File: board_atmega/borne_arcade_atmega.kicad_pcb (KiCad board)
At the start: 2 copper layers, 0 parts

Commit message: Layout and some modifications to ease layout
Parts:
- added C1: 100nF, SM0603, F.Cu at (301.1, 151.9)
- added C2: 1uF, SM0603, F.Cu at (295.6, 143.2)
- added C3: 100nF, SM0603, F.Cu at (298.3, 135.1)
- added C4: 100nF, SM0603, F.Cu at (300.4, 134.6)
- added C5: 1uF, SM0603, F.Cu at (307.4, 135.5)
- added C6: 22pF, SM0603, F.Cu at (306.5, 156.3)
- added C7: 10uF, SM0603, F.Cu at (311.4, 146.4)
- added C8: 22pF, SM0603, F.Cu at (298.4, 156.3)
- added FB1: FILTER, SM0603, F.Cu at (291.7, 139.2)
- added G1: LOGO, LOGO_135, F.Cu at (320.9, 153.0)
- added G2: LOGO_FOL, LOGO_FOL, F.Cu at (321.1, 134.8)
- added H1: HOLE_3MM, Hole_3mm, F.Cu at (283.6, 166.3)
- added H2: HOLE_3MM, Hole_3mm, F.Cu at (283.6, 123.2)
- added H3: HOLE_3MM, Hole_3mm, F.Cu at (325.6, 144.4)
- added P1: MUSB, USB_Mini, F.Cu at (282.3, 145.0)
- added P2: CONN_15, pin_array_15x1, F.Cu at (304.4, 163.2)
- added P3: CONN_15, pin_array_15x1, F.Cu at (312.1, 125.8)
- added R1: 22, SM0603, F.Cu at (291.4, 143.4)
- added R10: 100K, SM0603, F.Cu at (308.1, 166.3)
- added R11: 100K, SM0603, F.Cu at (310.8, 166.3)
- added R12: 100K, SM0603, F.Cu at (313.2, 166.3)
- added R13: 100K, SM0603, F.Cu at (315.8, 166.3)
- added R14: 100K, SM0603, F.Cu at (318.4, 166.3)
- added R15: 100K, SM0603, F.Cu at (320.9, 166.3)
- added R16: 100K, SM0603, F.Cu at (323.4, 166.3)
- added R17: 100K, SM0603, F.Cu at (323.6, 122.7)
- added R18: 100K, SM0603, F.Cu at (321.1, 122.7)
- added R19: 100K, SM0603, F.Cu at (318.5, 122.7)
- added R2: 22, SM0603, F.Cu at (292.1, 144.9)
- added R20: 100K, SM0603, F.Cu at (315.9, 122.7)
- added R21: 100K, SM0603, F.Cu at (313.4, 122.7)
- added R22: 100K, SM0603, F.Cu at (310.9, 122.7)
- added R23: 100K, SM0603, F.Cu at (308.4, 122.7)
- added R24: 100K, SM0603, F.Cu at (305.9, 122.7)
- added R25: 100K, SM0603, F.Cu at (303.4, 122.7)
- added R26: 100K, SM0603, F.Cu at (300.8, 122.7)
- added R27: 100K, SM0603, F.Cu at (298.1, 122.7)
- added R28: 100K, SM0603, F.Cu at (295.8, 122.7)
- added R29: 100K, SM0603, F.Cu at (293.1, 122.7)
- added R3: 10K, SM0603, F.Cu at (299.1, 151.6)
- added R4: 100K, SM0603, F.Cu at (292.9, 166.3)
- added R5: 100K, SM0603, F.Cu at (295.4, 166.3)
- added R6: 100K, SM0603, F.Cu at (297.9, 166.3)
- added R7: 100K, SM0603, F.Cu at (300.5, 166.3)
- added R8: 100K, SM0603, F.Cu at (303.1, 166.3)
- added R9: 100K, SM0603, F.Cu at (305.6, 166.2)
- added U1: ATMEGA32U4, TQFP44, F.Cu at (303.2, 142.8)
- added X1: QUARTZ_CMS_4, 7B_CMS4_Quartz, F.Cu at (302.4, 155.8)
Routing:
- net DGND: track 0.00 -> 305.0 mm, vias 0 -> 46
- net N-0000033: track 0.00 -> 31.5 mm
- net N-0000034: track 0.00 -> 29.0 mm
- net N-0000015: track 0.00 -> 28.3 mm
- net N-0000035: track 0.00 -> 26.7 mm
- net N-0000014: track 0.00 -> 25.7 mm
- net N-0000031: track 0.00 -> 24.3 mm
- net N-0000013: track 0.00 -> 23.2 mm
- net N-0000030: track 0.00 -> 23.2 mm
- net N-0000028: track 0.00 -> 22.9 mm
- net N-0000027: track 0.00 -> 22.6 mm
- net N-0000029: track 0.00 -> 22.6 mm
- net N-0000012: track 0.00 -> 21.1 mm
- net N-0000032: track 0.00 -> 20.8 mm
- net N-0000023: track 0.00 -> 20.1 mm
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- added copper zone on F.Cu, net /+5V
- added copper zone on B.Cu, net DGND
- added copper zone on F.Cu, net DGND
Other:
- board outline added: 50 x 50 mm
- net class Alim added: clearance 0.19304, trace_width 0.3048, via_dia 0.889, via_drill 0.508
- net class Default: clearance 0.254 -> 0.19304; trace_width 0.254 -> 0.2032; via_dia 0.889 -> 0.508; via_drill 0.635 -> 0.381
- rule trace_clearance: 0.254 -> 0.19304
- rule trace_min: 0.254 -> 0.2032
- rule via_min_drill: 0.508 -> 0.381
- rule via_min_size: 0.889 -> 0.508

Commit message: First version produced
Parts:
- added G3: LOGO_OSHW, OSHW_logo_silkscreen-front_6mm, F.Cu at (286.4, 131.8)
- moved G2 1.64 mm to (319.7, 135.6)
- moved G1 0.78 mm to (321.2, 152.3)
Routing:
- net DGND: track 305.0 -> 297.8 mm
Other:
- board text added: "+5V"
- board text added: "GND"
- board text added: "PB.0"
- board text added: "PB.1"
- board text added: "PB.2"
- board text added: "PB.3"
- board text added: "PB.4"
- board text added: "PB.5"
- board text added: "PB.6"
- board text added: "PB.7"
- board text added: "PC.6"
- board text added: "PC.7"
- board text added: "PD.0"
- board text added: "PD.1"
- board text added: "PD.2"
- board text added: "PD.3"
- board text added: "PD.4"
- board text added: "PD.5"
- board text added: "PD.6"
- board text added: "PD.7"
- board text added: "PE.2"
- board text added: "PE.6"
- board text added: "PF.0"
- board text added: "PF.1"
- board text added: "PF.4"
- board text added: "PF.5"
- board text added: "PF.6"
- board text added: "PF.7"
- board text added: "Techno-Innov Borne Arcade v0.1"

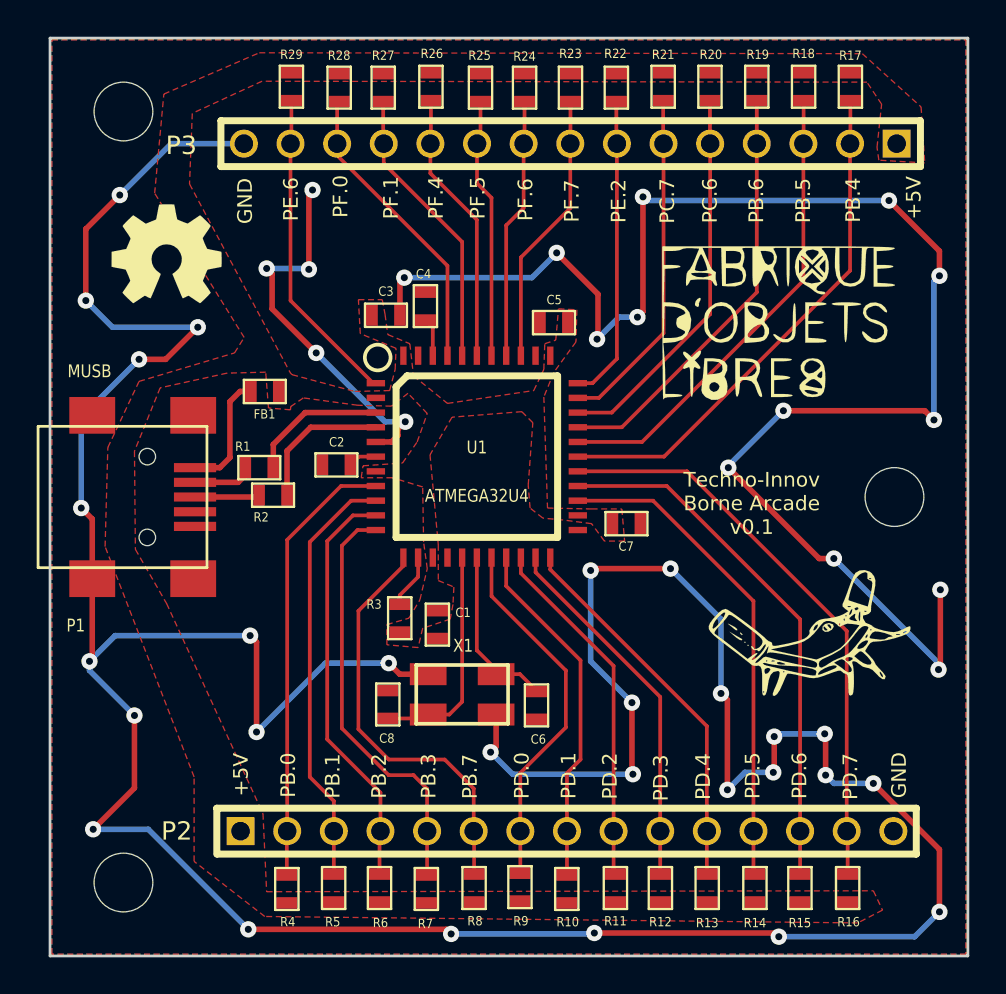
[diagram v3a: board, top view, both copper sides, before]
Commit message: Nev revision v0.2 : - Adding the switches for reset and ISP mode selection - Addind reset pin - Changed USB connector to micro-USB (was mini-USB) - Adding power led - Using "arduino" names on top silkscreen and "Atmel" ones on bottom silkscreen
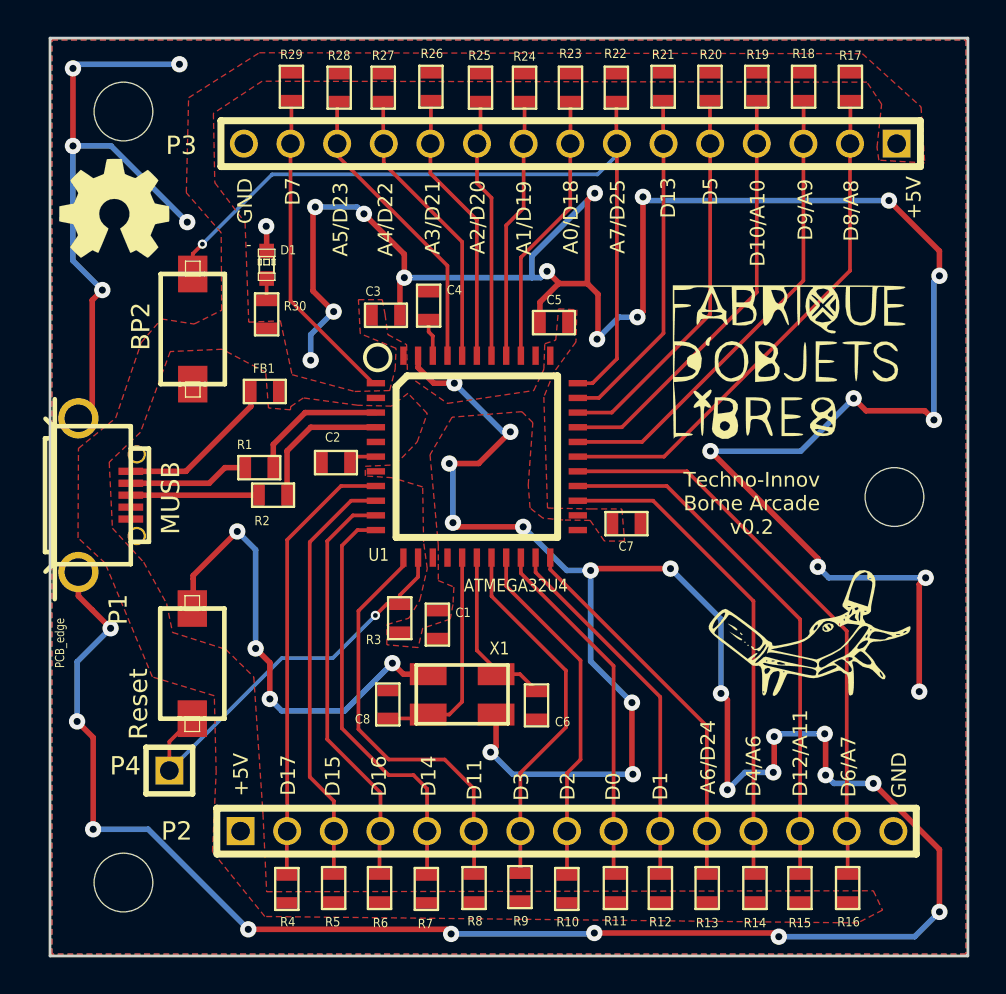
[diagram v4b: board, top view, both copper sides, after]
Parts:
- added D1: LED, LED-0603, F.Cu at (291.8, 132.3)
- added P4: CONN_1, pin_1x1, F.Cu at (286.5, 159.9)
- added R30: 1k, SM0603, F.Cu at (291.8, 135.1)
- added SW1: Reset, SWITCH_CMS, F.Cu at (287.8, 154.1)
- added SW2: BP2, SWITCH_CMS, F.Cu at (287.8, 135.8)
- P1: footprint USB_Mini -> USB_micro_AB_Picots
- moved G3 3.77 mm to (283.5, 129.3)
- moved G2 2.20 mm to (320.3, 137.7)
- moved P1 2.10 mm to (284.4, 144.9)
- moved C4 0.18 mm to (300.6, 134.6)
- moved C2 0.13 mm to (295.6, 143.1)
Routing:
- net DGND: track 297.8 -> 327.5 mm, vias 46 -> 53
- net N-0000024: track 16.7 -> 43.8 mm, vias 0 -> 1
- net N-0000019: track 2.95 -> 22.6 mm, vias 0 -> 1
- net /D+_USB: track 3.53 -> 6.99 mm
- net /D-_USB: track 3.31 -> 6.59 mm
- net /+5V_USB: track 6.54 -> 8.82 mm
- net N-0000018: track 0.00 -> 1.19 mm
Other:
- board text added: "A0/D18"
- board text added: "A1/D19"
- board text added: "A2/D20"
- board text added: "A3/D21"
- board text added: "A4/D22"
- board text added: "A5/D23"
- board text added: "A6/D24"
- board text added: "A7/D25"
- board text added: "D0"
- board text added: "D1"
- board text added: "D10/A10"
- board text added: "D11"
- board text added: "D12/A11"
- board text added: "D13"
- board text added: "D14"
- board text added: "D15"
- board text added: "D16"
- board text added: "D17"
- board text added: "D2"
- board text added: "D3"
- board text added: "D4/A6"
- board text added: "D5"
- board text added: "D6/A7"
- board text added: "D7"
- board text added: "D8/A8"
- board text added: "D9/A9"
- board text added: "MISO / PB.3"
- board text added: "MOSI / PB.2"
- board text added: "SCLK / PB.1"
- board text added: "Slave sel / PB.0"
- board text added: "Techno-Innov Borne Arcade v0.2"
- board text removed: "PB.0"
- board text removed: "PB.1"
- board text removed: "PB.2"
- board text removed: "PB.3"
- board text removed: "Techno-Innov Borne Arcade v0.1"
